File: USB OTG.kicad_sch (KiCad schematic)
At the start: 24 parts, among them J4 USB_OTG, Q1 Q_PNP_BEC, U1 rv1126/rv1109

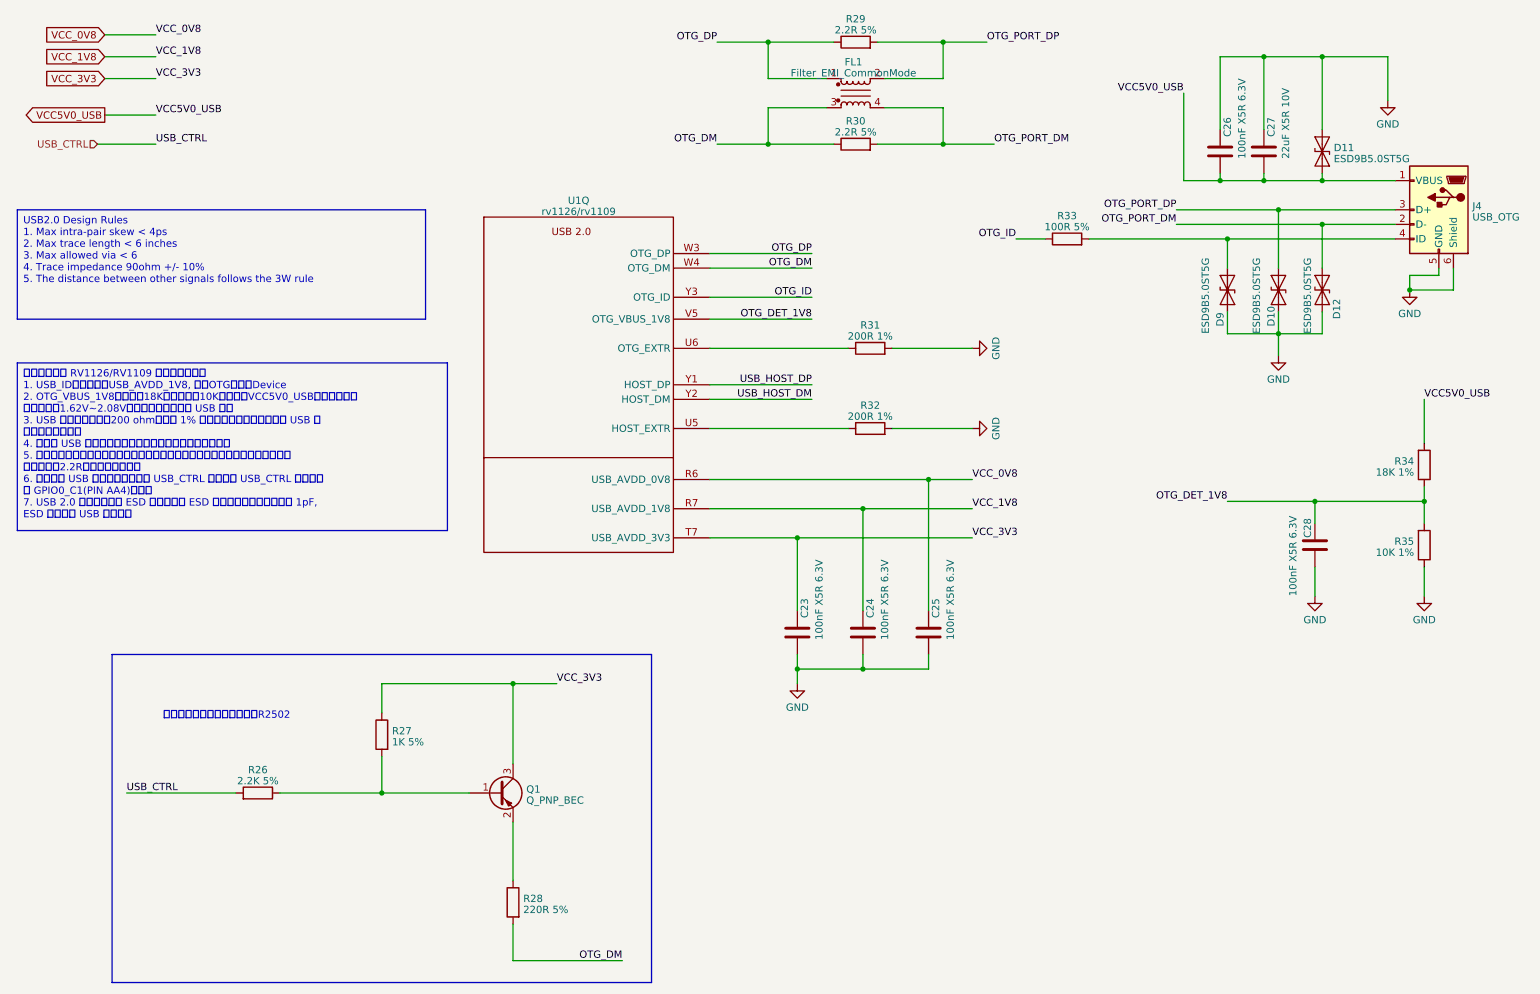
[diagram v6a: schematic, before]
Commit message: fix some ERCs
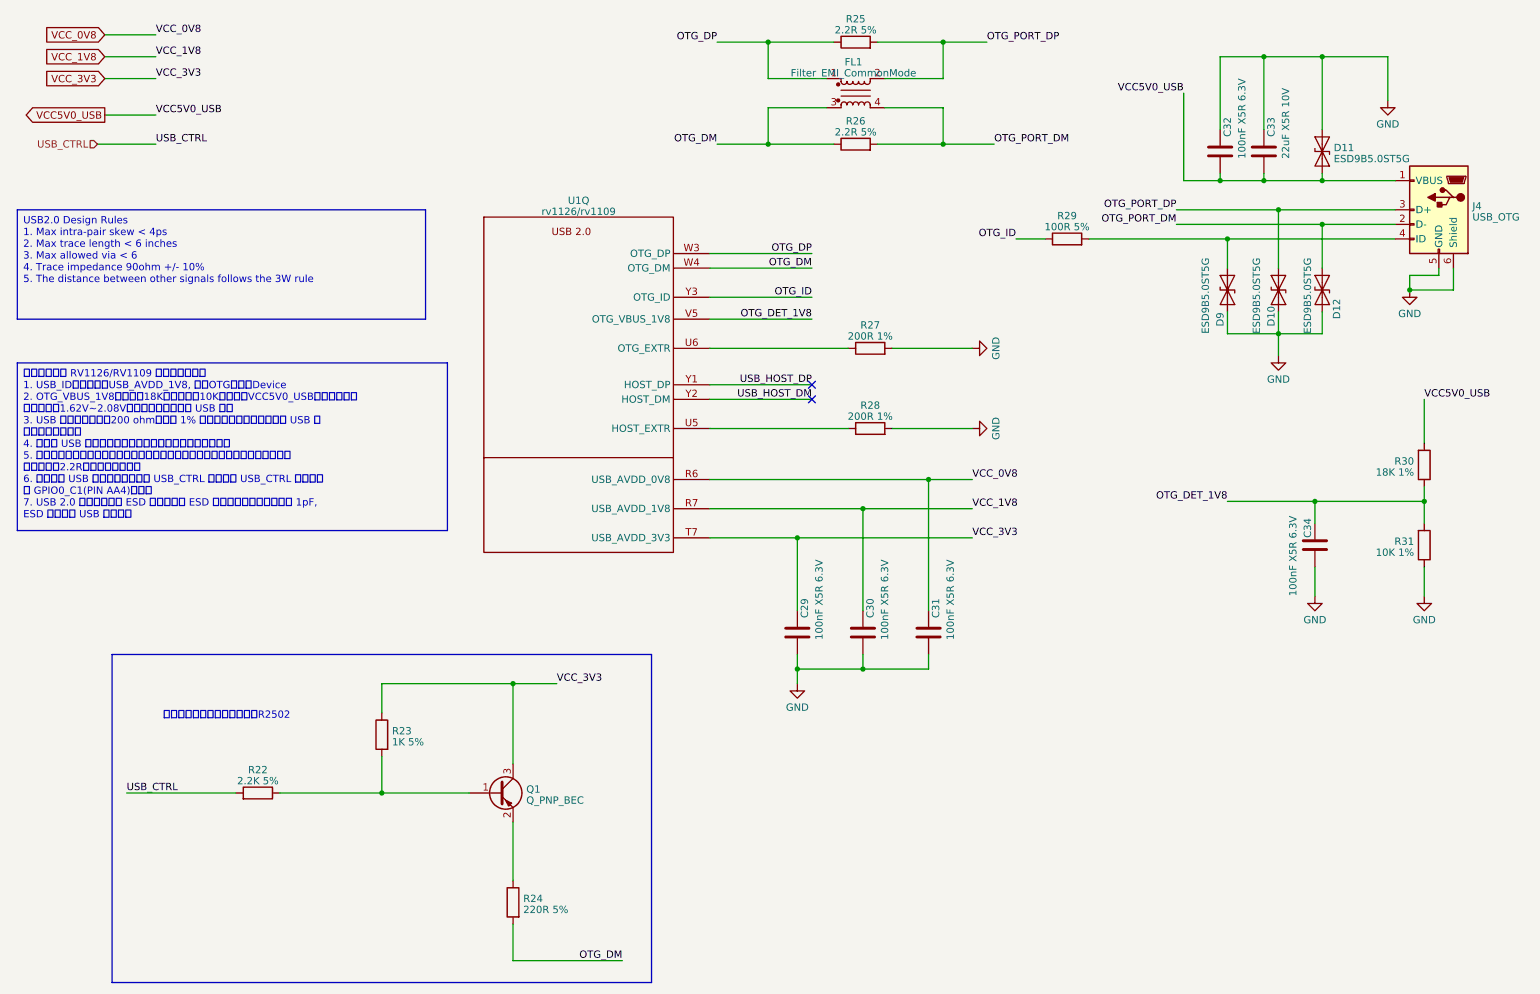
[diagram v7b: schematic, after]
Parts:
- renumbered C23 to C29, C24 to C30, C25 to C31, C26 to C32, C27 to C33, C28 to C34, R26 to R22, R27 to R23, R28 to R24, R29 to R25, R30 to R26, R31 to R27, R32 to R28, R33 to R29, R34 to R30, R35 to R31
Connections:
- no-connect marks 0 -> 2

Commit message: added VDD Logic
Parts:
- R29: LCSC (none) -> C25138; Model (none) -> 0402WGJ0101TCE; Vendor (none) -> UNI-ROYAL(厚声)
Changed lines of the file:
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@@
+      (effects (font (size 1.27 1.27)) hide)
+    )
+    (property "Description" "电阻类型: 厚膜电阻 阻值: 100Ω 精度: ±5% 功率: 1/16W 温度系数: ±100ppm/℃ 最大工作电压: 50V 工作温度" (at 199.39 55.88 0)
+      (effects (font (size 1.27 1.27)) hide)
+    )
+    (property "LCSC" "C25138" (at 199.39 55.88 0)
+      (effects (font (size 1.27 1.27)) hide)
+    )
+    (property "Model" "0402WGJ0101TCE" (at 199.39 55.88 0)
+      (effects (font (size 1.27 1.27)) hide)
+    )
+    (property "Vendor" "UNI-ROYAL(厚声)" (at 199.39 55.88 0)
       (effects (font (size 1.27 1.27)) hide)
     )
